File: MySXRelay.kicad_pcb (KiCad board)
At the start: 4 copper layers, 36 x 36.6 mm, 65 parts, among them J1 AVR ISP, J2 PRG/BL0942, J3 Relay, Q1 2N7002, U2 BL0942, U3 BP2525X, U4 Si8642BB-B-IS1, U5 MCP1703Ax-180xxTT, U6 ATmega328PB-A, U7 AT25xxx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

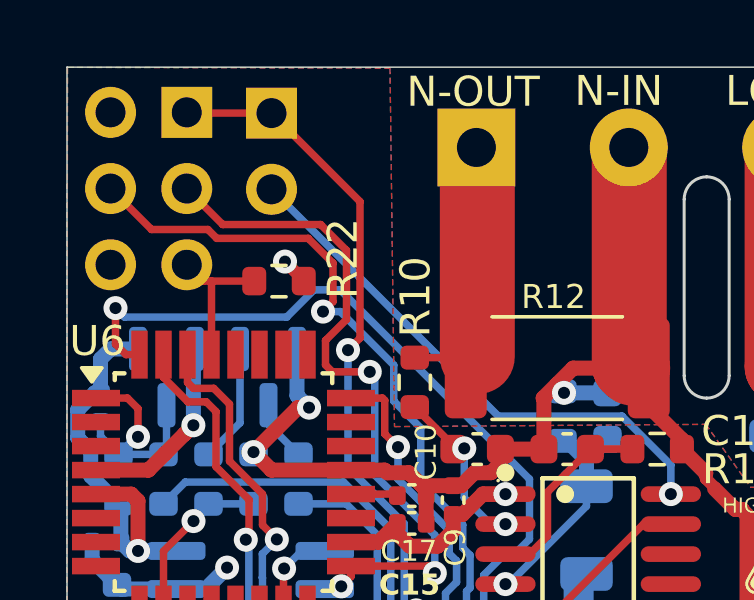
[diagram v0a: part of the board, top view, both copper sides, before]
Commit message: remove BL0942 TX pin jumper and add pull up resistor
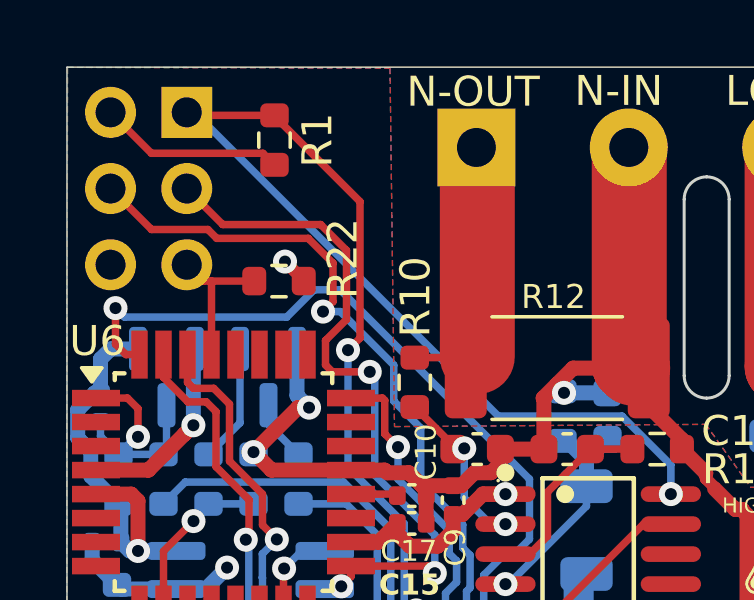
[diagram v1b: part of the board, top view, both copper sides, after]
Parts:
- removed J2: PRG/BL0942, Connector_PinHeader_2.54mm:PinHeader_1x02_P2.54mm_Vertical
- added R1: 10k, Resistor_SMD:R_0603_1608Metric, F.Cu at (153.5, 84.9)
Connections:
- J1 pad 1: MISO -> BL0942_TX
- U6 pad 16: MISO -> BL0942_TX
- U7 pad 2: MISO -> BL0942_TX
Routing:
- net BL0942_TX: track 18.1 -> 67.3 mm, vias 1 -> 5
- net MISO: track 45.3 -> 0.00 mm, vias 4 -> 0
- net +3V3: track 104.0 -> 110.1 mm

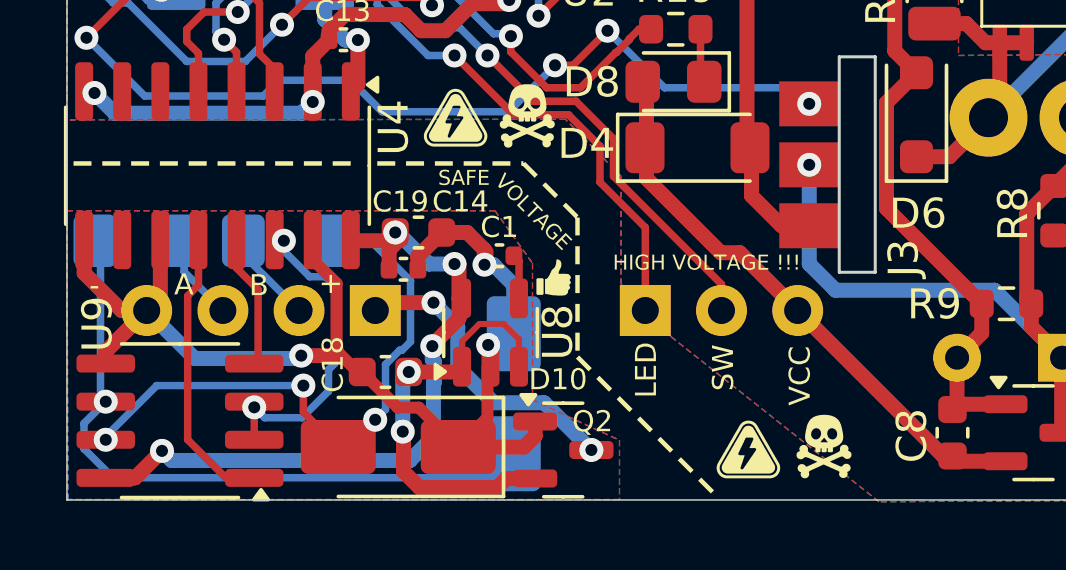
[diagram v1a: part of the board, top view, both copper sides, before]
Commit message: change RS485 interface LDO package to sot-89
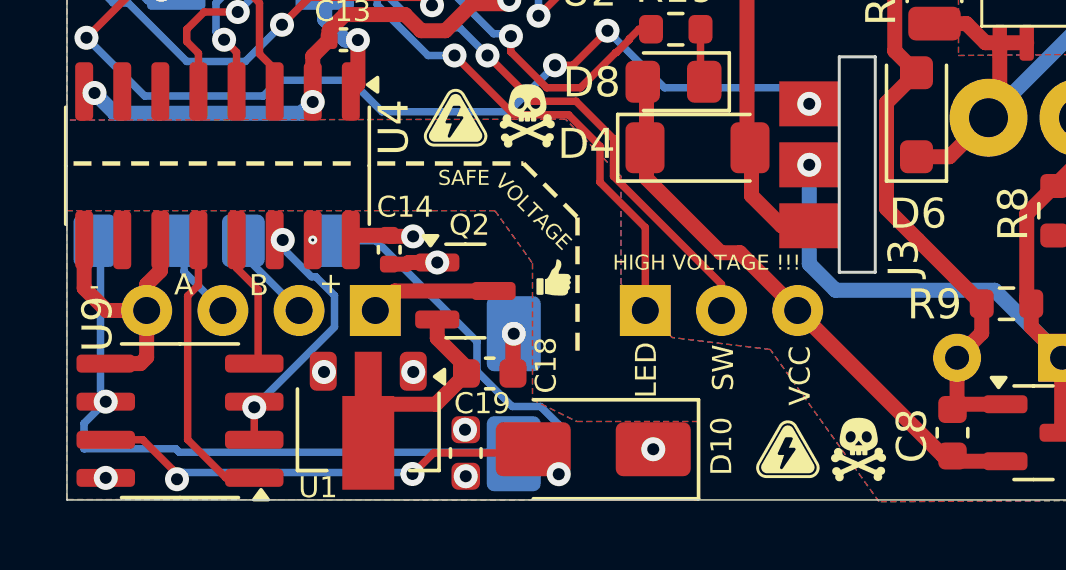
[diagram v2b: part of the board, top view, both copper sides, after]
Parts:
- removed C1: 100p, Capacitor_SMD:C_0402_1005Metric
- removed U8: AP2202K-5.0, Package_TO_SOT_SMD:SOT-23-5
- added U1: AP2204RA-5.0, Package_TO_SOT_SMD:SOT-89-3, F.Cu at (156.6, 116.7)
- moved C19 7.52 mm to (159.9, 117.5), turned to 90 degrees
- moved D10 6.50 mm to (164.1, 117.3)
- moved Q2 6.22 mm to (159.9, 112.1)
- moved C18 3.48 mm to (160.7, 114.8), turned to 0 degrees
- moved C14 0.81 mm to (157.3, 110.7), turned to -90 degrees
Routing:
- net Net-(D10-A2): track 20.0 -> 28.9 mm
- net Net-(Q2-S): track 14.1 -> 6.82 mm, vias 2 -> 0
- net Net-(Q2-D): track 10.1 -> 4.21 mm, vias 2 -> 0
- net GND1: track 41.8 -> 46.0 mm, vias 3 -> 6
- net Net-(U4-B1): track 10.7 -> 9.03 mm
- net Net-(U8-BYP): track 1.50 -> 0.00 mm
- net +5VD: track 23.5 -> 22.6 mm
- net Net-(D9-A2): track 22.4 -> 21.8 mm
- added copper zone on In2.Cu, net +5VD
- added copper zone on In1.Cu, net GND1

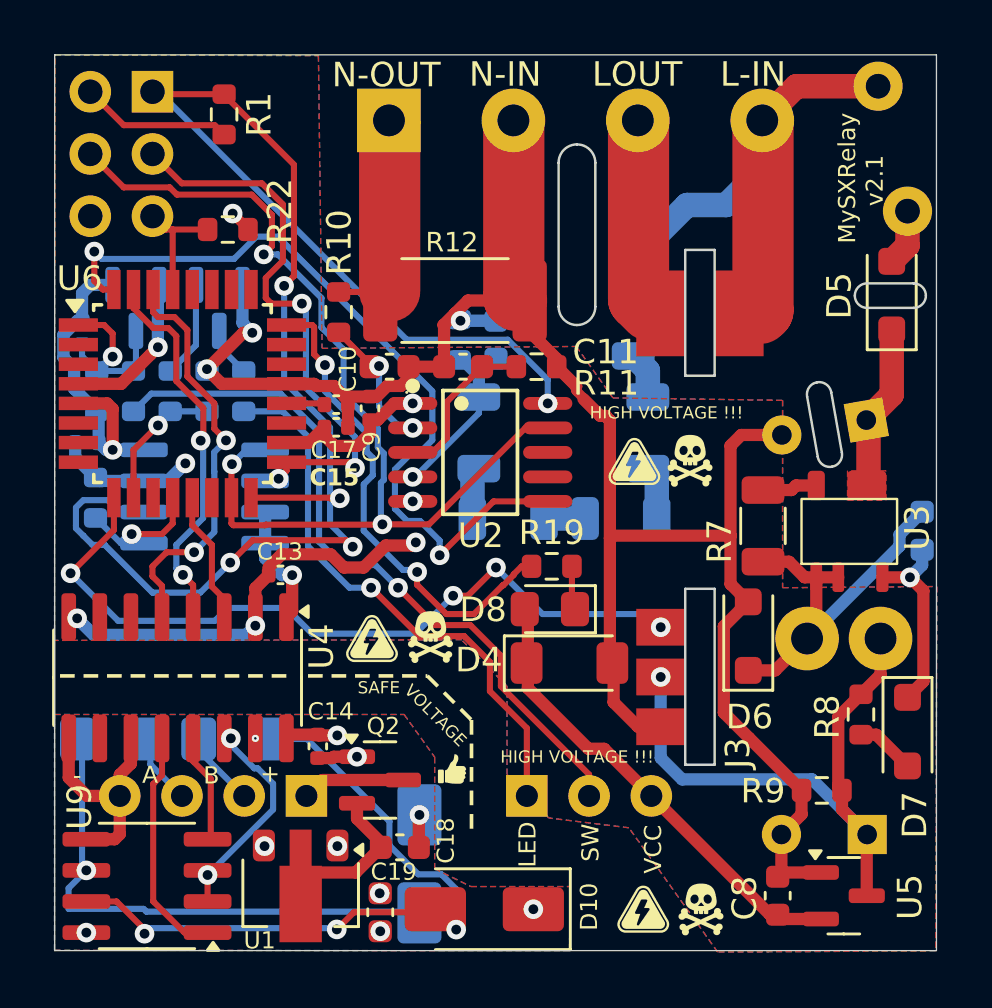
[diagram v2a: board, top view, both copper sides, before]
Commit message: shrink PCB to fit 40mmx40mm  HM-1551V1WH case
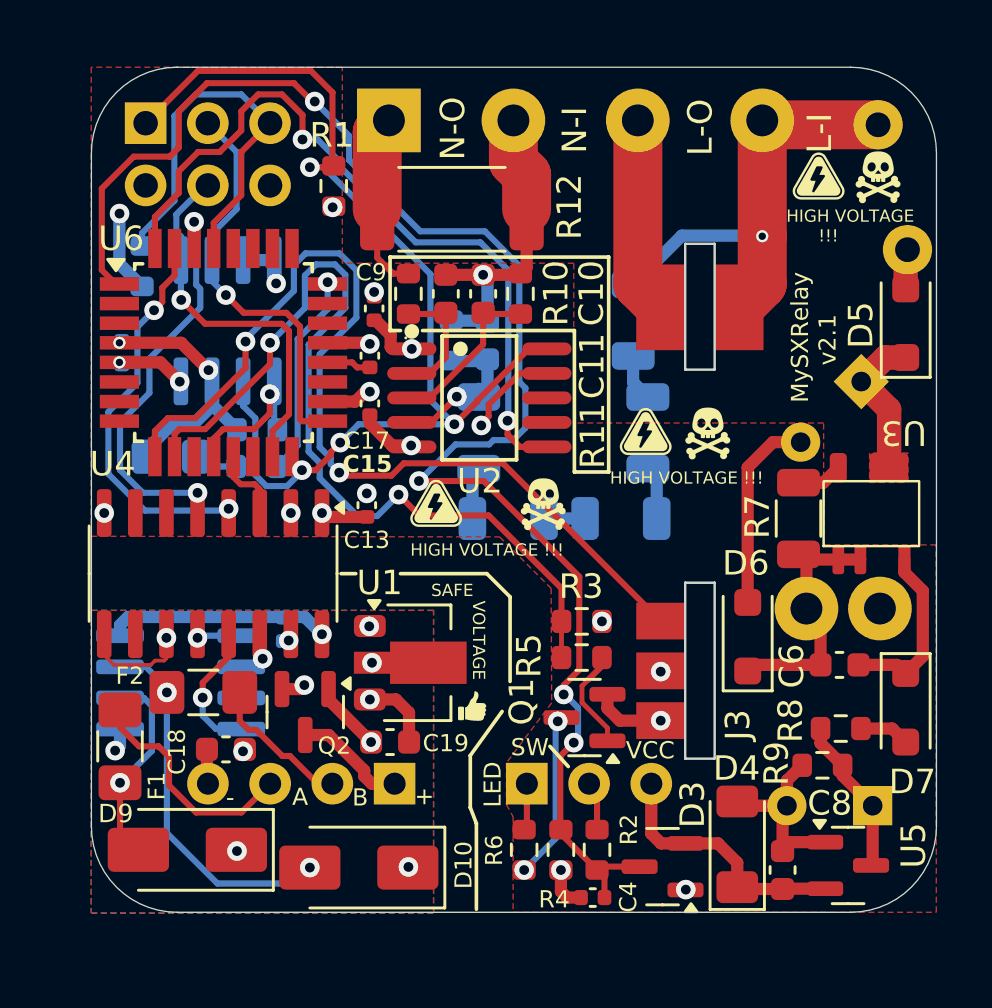
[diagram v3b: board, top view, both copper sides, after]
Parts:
- C14, D8, R19, R22, U9: moved to B.Cu
- C4, C6, D3, D9, F1, F2, Q1, R2, R3, R4, R5, R6: moved to F.Cu
- moved D3 31.3 mm to (171.4, 115.6), turned to 180 degrees
- moved C4 31.1 mm to (168.6, 116.9), turned to 180 degrees
- moved R4 26.6 mm to (167.2, 114.9)
- moved R2 26.6 mm to (168.7, 114.9), turned to -90 degrees
- moved Q1 22.4 mm to (168.2, 109.5), turned to 180 degrees
- moved R6 21.9 mm to (165.8, 114.9), turned to -90 degrees
- moved R5 20.0 mm to (168.1, 107.1), turned to 0 degrees
- moved R3 18.0 mm to (168.1, 105.6), turned to 0 degrees
- moved D8 16.7 mm to (151.3, 98.9)
- moved R19 12.7 mm to (154.8, 99.3), turned to 0 degrees
- moved U1 10.6 mm to (161.4, 107.3), turned to 0 degrees
- moved D4 10.1 mm to (174.4, 114.7), turned to 90 degrees
- moved D9 9.49 mm to (152.0, 114.9), turned to 180 degrees
- moved U9 8.42 mm to (151.7, 108.1)
- moved C18 8.15 mm to (153.6, 110.8), turned to 180 degrees
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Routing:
- net D3: track 7.94 -> 64.3 mm, vias 1 -> 4
- net D6: track 5.65 -> 36.6 mm, vias 1 -> 2
- net N_IN: track 162.1 -> 131.6 mm, vias 8 -> 13
- net /MCU/SW: track 29.6 -> 2.01 mm, vias 1 -> 0
- net BL0942_TX: track 67.3 -> 45.4 mm, vias 5 -> 4
- net +3V3: track 110.1 -> 88.7 mm, vias 5 -> 8
- net /MCU/LED: track 23.1 -> 1.92 mm, vias 1 -> 0
- net Net-(D10-A2): track 28.9 -> 15.2 mm, vias 3 -> 2
- net Net-(D9-A2): track 21.8 -> 8.16 mm
- net RST: track 4.93 -> 16.7 mm
- net /MCU/A1: track 20.0 -> 8.46 mm, vias 2 -> 1
- net Net-(U4-B3): track 9.55 -> 1.82 mm, vias 0 -> 1
- net D5: track 31.7 -> 39.1 mm, vias 4 -> 2
- net SCK: track 23.8 -> 16.7 mm, vias 3 -> 1
- net +5VD: track 22.6 -> 15.6 mm, vias 4 -> 2
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- removed copper zone on B.Cu, net N_IN
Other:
- board size 36 x 36.6 mm -> 34.5 x 34.5 mm
- board text added: "L-I"
- board text added: "L-O"
- board text added: "N-I"
- board text added: "N-O"
- board text removed: "L-IN"
- board text removed: "LOUT"
- board text removed: "N-IN"
- board text removed: "N-OUT"

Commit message: add BOM + update schematic parts descriptions
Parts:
- Q2: value ~ -> BSS84A
- U5: value MCP1703Ax-180xxTT -> AP2127N-3.3
- X1: value ~ -> RS485
- X2: value ~ -> Mains
- X3: value ~ -> Switch/LED
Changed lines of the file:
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@@
 			)
 		)
-		(property "Value" "MCP1703Ax-180xxTT"
+		(property "Value" "AP2127N-3.3"
 			(at 0 2.4 0)
 			(layer "F.Fab")
@@
 			)
 		)
-		(property "Datasheet" "http://ww1.microchip.com/downloads/en/DeviceDoc/20005122B.pdf"
+		(property "Datasheet" "https://www.diodes.com/assets/Datasheets/AP2127.pdf"
 			(at 0 0 0)
 			(layer "F.Fab")
@@
 			)
 		)
-		(property "Description" "Low Quiescent Current LDO Regulator, 1.8V, 250mA, Vin<=16V, SOT-23"
+		(property "Description" "300mA low dropout linear regulator, shutdown pin, 2.5V-6V input voltage, 3.3V fixed positive output, SOT-23 package"
 			(at 0 0 0)
 			(layer "F.Fab")
@@
 			)
 		)
-		(property "Value" "~"
+		(property "Value" "BSS84A"
 			(at 0 2.4 90)
 			(layer "F.Fab")
@@
 			)
 		)
-		(property "Value" "~"
+		(property "Value" "Switch/LED"
 			(at 3.4485 -6.042 90)
 			(layer "B.Fab")
@@
 			)
 		)
-		(property "Value" "~"
+		(property "Value" "Mains"
 			(at 7.62 -5.66 0)
 			(layer "B.Fab")
@@
 			)
 		)
-		(property "Value" "~"
+		(property "Value" "RS485"
 			(at 3.4485 -1.085 90)
 			(layer "B.Fab")
